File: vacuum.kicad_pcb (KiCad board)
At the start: 2 copper layers, 67 parts, among them J1 к БП, J10 геркон шибера 1, J11 запасной, J12 запасной, J13 к БП, J2 нагрузка, J3 нагрузка, J4 геркон клапана 0, J5 нагрузка, J6 нагрузка, J7 к БП, J8 геркон клапана 1, J9 геркон шибера 0, Q1 IRF740, Q2 IRF740, Q3 IRF740, Q4 IRF740, SW1 Кнопка, SW2 Кнопка, SW3 Кнопка, SW4 Выключить автоматику, SW5 Кнопка, U1 PC817, U10 PC817, U2 PC817, U3 PC817, U4 PC817, U5 PC817, U6 PC817, U7 PC817, U8 PC817, U9 PC817

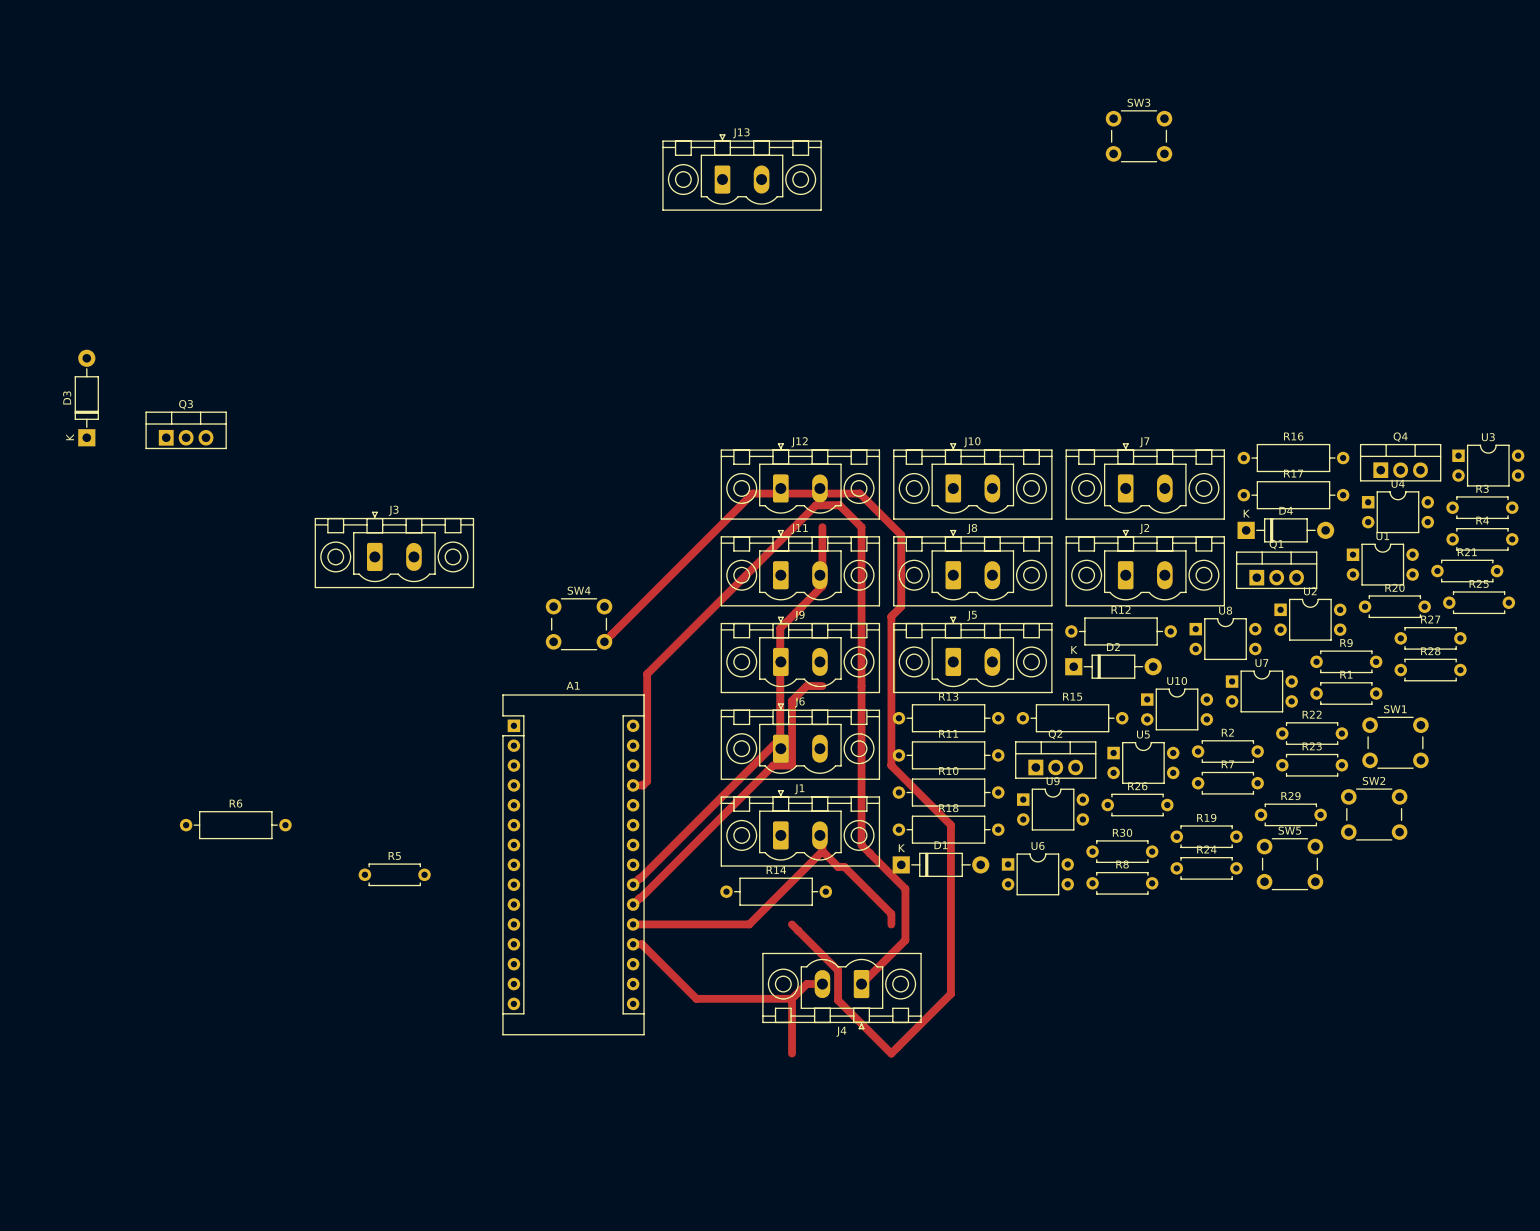
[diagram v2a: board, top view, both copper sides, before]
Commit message: some scheme bags removed
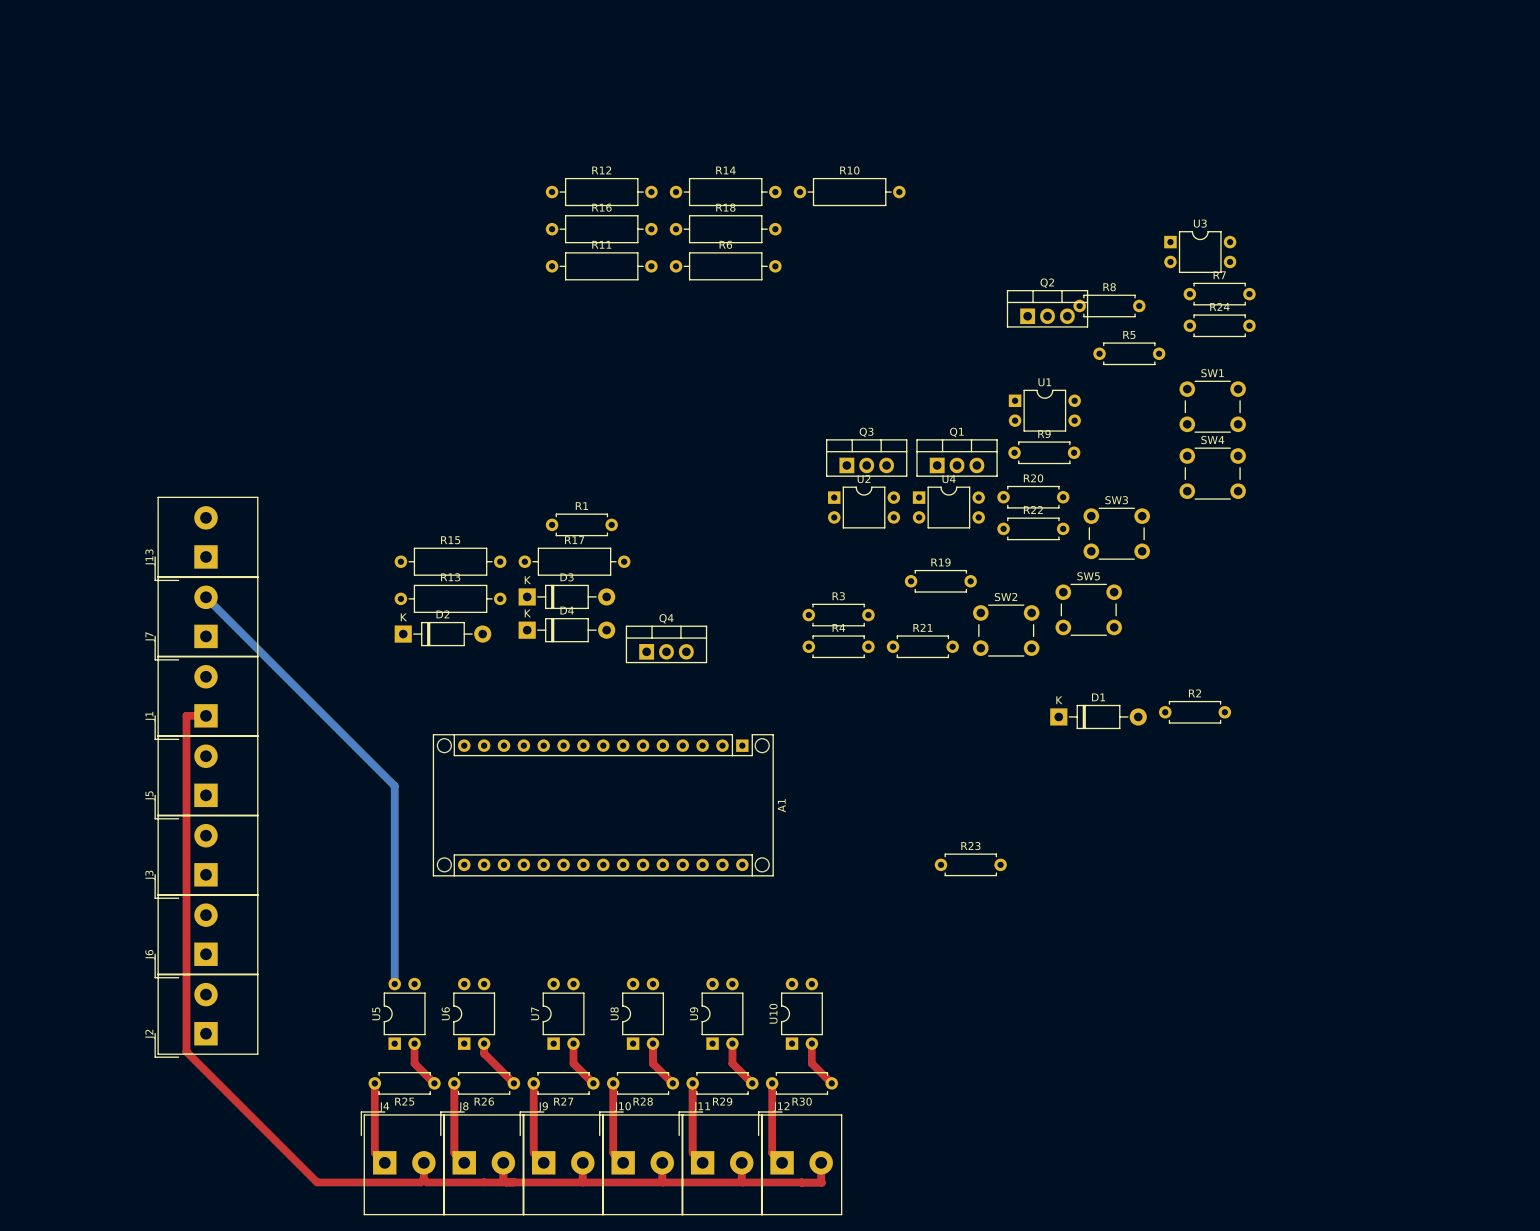
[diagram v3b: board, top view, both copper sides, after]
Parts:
- A1: footprint Module:Arduino_Nano -> Module:Arduino_Nano_WithMountingHoles
- J1, J10, J11, J12, J13, J2, J3, J4, J5, J6, J7, J8, J9: footprint Connector_Phoenix_MSTB:PhoenixContact_MSTBV_2,5_2-GF_1x02_P5.00mm_Vertical_ThreadedFlange -> TerminalBlock_Altech:Altech_AK300_1x02_P5.00mm_45-Degree
- moved R25 143.6 mm to (102.9, 149.9), turned to 180 degrees
- moved J2 131.4 mm to (73.7, 143.5), turned to 90 degrees
- moved J7 119.1 mm to (73.7, 92.7), turned to 90 degrees
- moved R27 117.9 mm to (123.2, 149.9), turned to 180 degrees
- moved R5 115.2 mm to (187.9, 56.6)
- moved R28 107.0 mm to (133.3, 149.9), turned to 180 degrees
- moved R1 100.1 mm to (117.9, 78.5)
- moved U5 99.1 mm to (97.8, 144.8), turned to 90 degrees
- moved U7 98.3 mm to (118.1, 144.8), turned to 90 degrees
- moved J8 97.8 mm to (106.7, 160.0)
- moved J5 97.1 mm to (73.7, 113.0), turned to 90 degrees
- moved Q4 96.7 mm to (130.0, 94.7)
- moved J10 96.0 mm to (127.0, 160.0)
- moved R6 95.0 mm to (133.8, 45.4)
- moved R16 93.2 mm to (117.9, 40.6)
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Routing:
- net +5V: track 116.3 -> 59.4 mm
- net Net-(A1-Pad22): track 55.8 -> 0.00 mm
- net Net-(A1-Pad20): track 42.4 -> 0.00 mm
- net Net-(A1-Pad21): track 40.6 -> 0.00 mm
- net Net-(A1-Pad19): track 35.7 -> 0.00 mm
- net Net-(J9-Pad1): track 0.00 -> 10.7 mm
- net Net-(J8-Pad1): track 0.00 -> 10.7 mm
- net Net-(J11-Pad1): track 0.00 -> 10.7 mm
- net Net-(J4-Pad1): track 0.00 -> 10.7 mm
- net Net-(J10-Pad1): track 0.00 -> 10.7 mm
- net Net-(J12-Pad1): track 0.00 -> 10.7 mm
- net Earth: track 142.9 -> 149.9 mm
- net Net-(R26-Pad1): track 0.00 -> 6.66 mm
- net Net-(R25-Pad1): track 0.00 -> 6.13 mm
- net Net-(R30-Pad1): track 0.00 -> 6.13 mm
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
